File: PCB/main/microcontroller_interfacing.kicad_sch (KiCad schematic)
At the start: 12 parts, among them IC3 M24C02-WMN6TP, J6 Conn_01x01_Female, J7 Conn_01x01_Female, J8 Conn_01x01_Female, U4 CH340G, Y1 Crystal

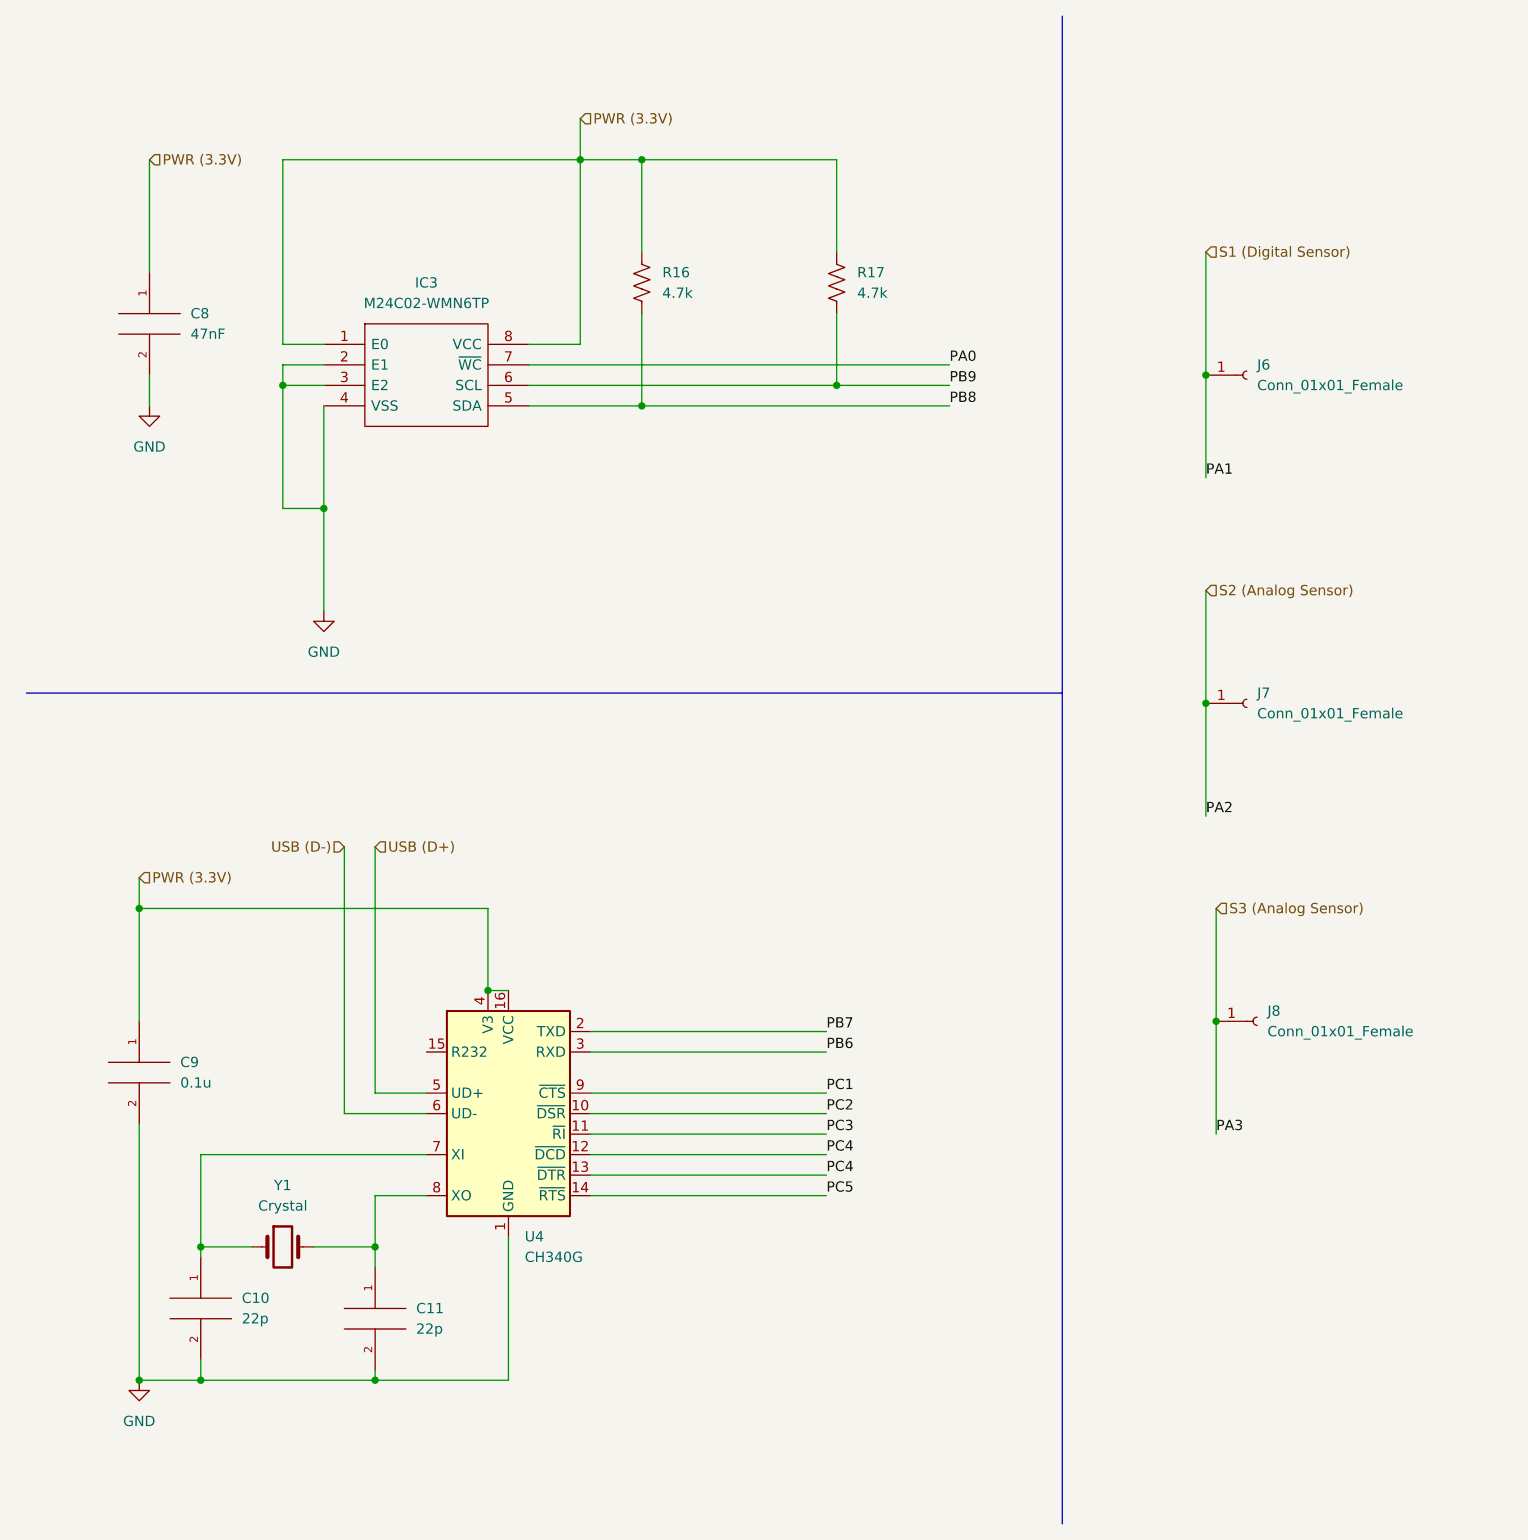
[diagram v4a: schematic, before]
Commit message: Power v0.1, Sensing v0.1, uC Control v0.1, ERC
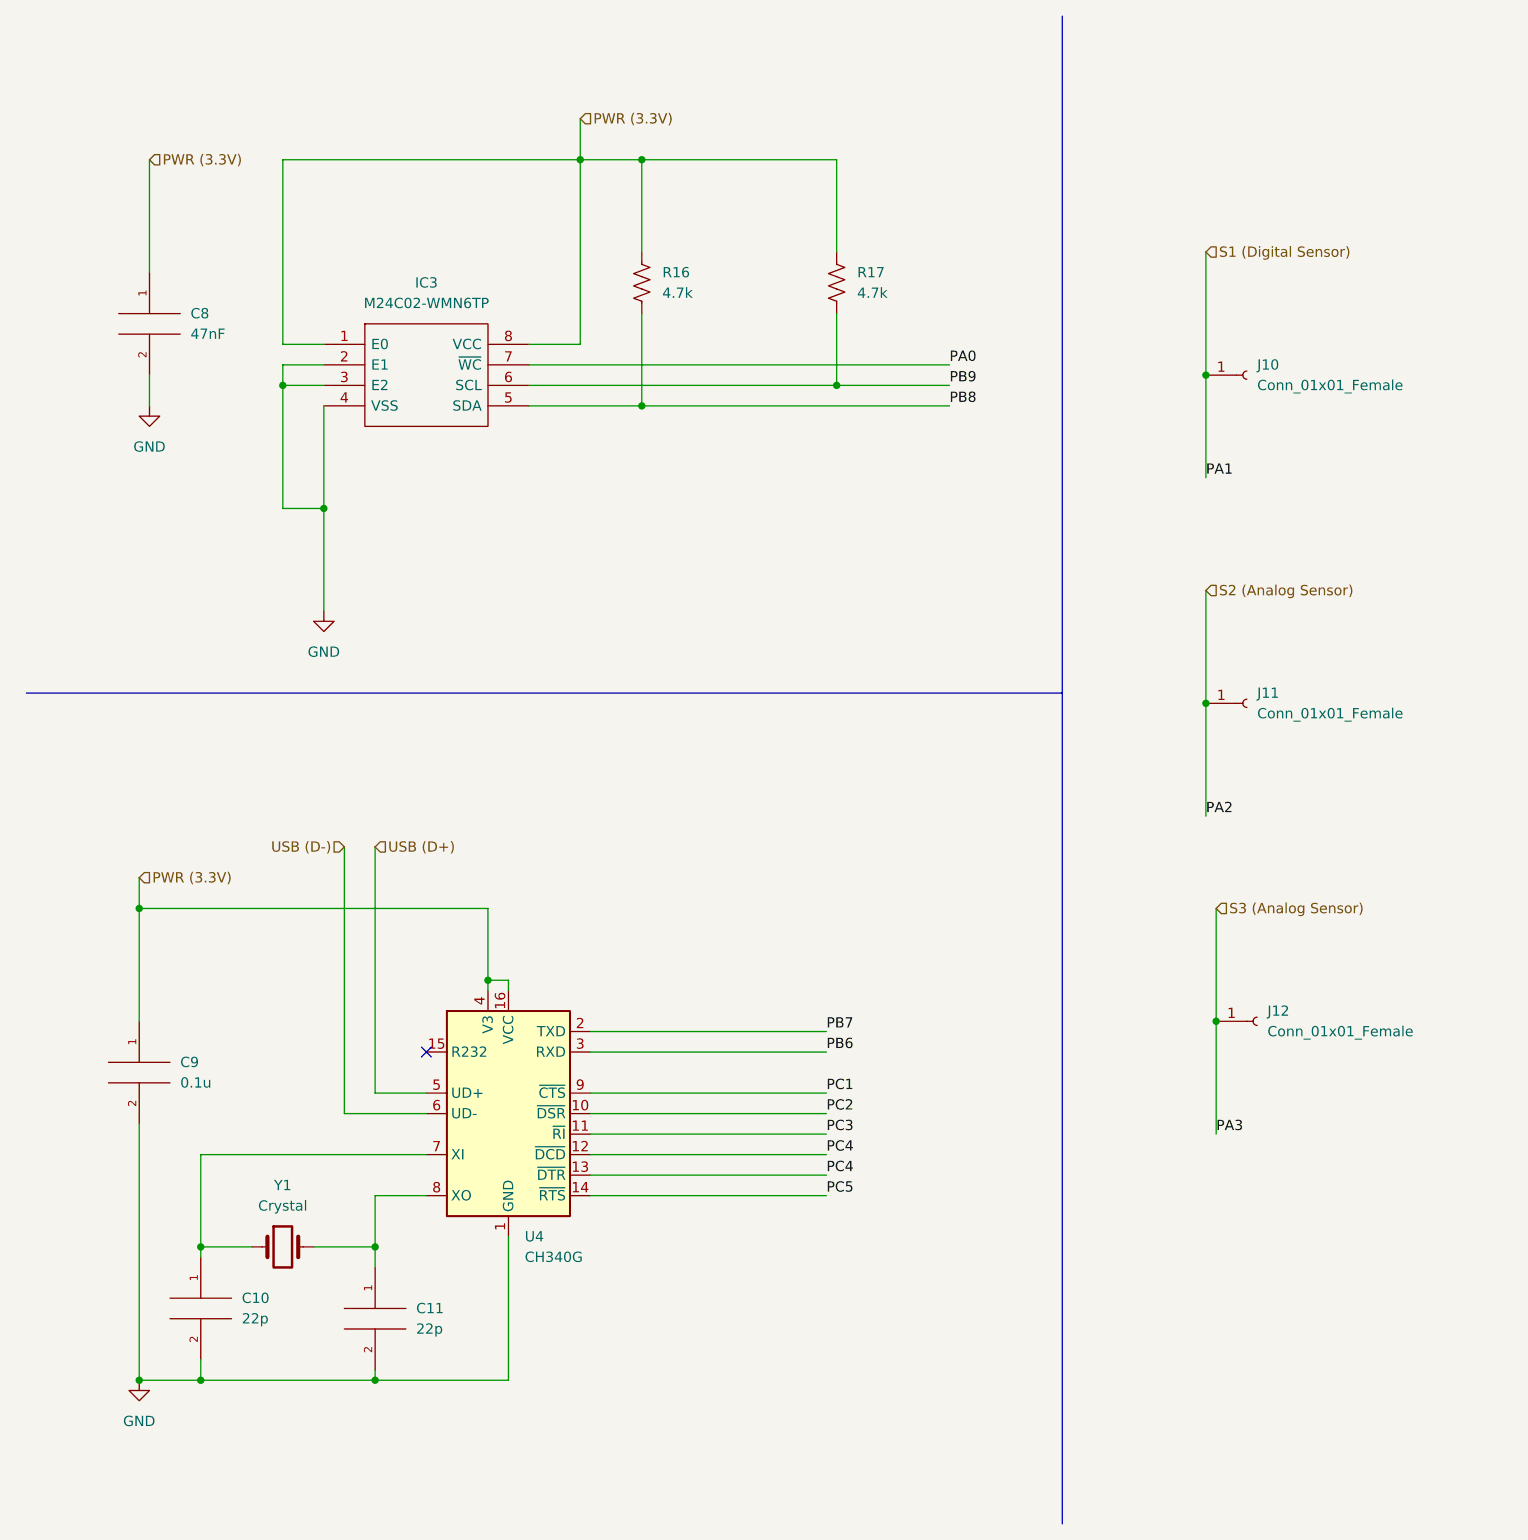
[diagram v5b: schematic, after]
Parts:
- renumbered J6 to J10, J7 to J11, J8 to J12
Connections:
- no-connect marks 0 -> 1
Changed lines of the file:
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@@
   (junction (at 157.48 55.88) (diameter 0) (color 0 0 0 0)
   )
+  (junction (at 68.58 130.81) (diameter 0) (color 0 0 0 0)
+  )
   (junction (at 111.76 57.15) (diameter 0) (color 0 0 0 0)
   )
   (junction (at 80.01 29.21) (diameter 0) (color 0 0 0 0)
   )
-  (junction (at 68.58 132.08) (diameter 0) (color 0 0 0 0)
-  )
   (junction (at 25.4 180.34) (diameter 0) (color 0 0 0 0)
   )
@@
   (junction (at 54.61 180.34) (diameter 0) (color 0 0 0 0)
   )
+  (no_connect (at 60.96 139.7))
   (wire (pts (xy 48.26 52.07) (xy 43.18 52.07))
     (stroke (width 0) (type default) (color 0 0 0 0))
@@
     (stroke (width 0) (type default) (color 0 0 0 0))
   )
-  (wire (pts (xy 68.58 132.08) (xy 71.12 132.08))
-    (stroke (width 0) (type default) (color 0 0 0 0))
-  )
   (wire (pts (xy 111.76 29.21) (xy 87.63 29.21))
     (stroke (width 0) (type default) (color 0 0 0 0))
@@
     (stroke (width 0) (type default) (color 0 0 0 0))
   )
+  (wire (pts (xy 71.12 130.81) (xy 71.12 132.08))
+    (stroke (width 0) (type default) (color 0 0 0 0))
+  )
   (wire (pts (xy 33.02 163.83) (xy 39.37 163.83))
     (stroke (width 0) (type default) (color 0 0 0 0))
@@
     (stroke (width 0) (type default) (color 0 0 0 0))
   )
-  (wire (pts (xy 68.58 121.92) (xy 68.58 132.08))
+  (wire (pts (xy 68.58 121.92) (xy 68.58 130.81))
     (stroke (width 0) (type default) (color 0 0 0 0))
   )
@@
     (stroke (width 0) (type default) (color 0 0 0 0))
   )
+  (wire (pts (xy 68.58 130.81) (xy 71.12 130.81))
+    (stroke (width 0) (type default) (color 0 0 0 0))
+  )
   (wire (pts (xy 81.28 152.4) (xy 110.49 152.4))
     (stroke (width 0) (type default) (color 0 0 0 0))
@@
   )
   (wire (pts (xy 46.99 163.83) (xy 54.61 163.83))
+    (stroke (width 0) (type default) (color 0 0 0 0))
+  )
+  (wire (pts (xy 68.58 130.81) (xy 68.58 132.08))
     (stroke (width 0) (type default) (color 0 0 0 0))
   )
@@
   (symbol (lib_id "power:GND") (at 26.67 59.69 0) (unit 1)
     (in_bom yes) (on_board yes) (fields_autoplaced)
-    (property "Reference" "#PWR038" (id 0) (at 26.67 66.04 0)
+    (property "Reference" "#PWR040" (id 0) (at 26.67 66.04 0)
       (effects (font (size 1.27 1.27)) hide)
     )
@@
   (symbol (lib_id "power:GND") (at 25.4 180.34 0) (unit 1)
     (in_bom yes) (on_board yes) (fields_autoplaced)
-    (property "Reference" "#PWR040" (id 0) (at 25.4 186.69 0)
+    (property "Reference" "#PWR042" (id 0) (at 25.4 186.69 0)
       (effects (font (size 1.27 1.27)) hide)
     )
@@
   (symbol (lib_id "Connector:Conn_01x01_Female") (at 162.56 96.52 0) (unit 1)
     (in_bom yes) (on_board yes) (fields_autoplaced)
-    (property "Reference" "J7" (id 0) (at 163.83 95.2499 0)
+    (property "Reference" "J11" (id 0) (at 163.83 95.2499 0)
       (effects (font (size 1.27 1.27)) (justify left))
     )
@@
   (symbol (lib_id "Connector:Conn_01x01_Female") (at 163.83 135.89 0) (unit 1)
     (in_bom yes) (on_board yes) (fields_autoplaced)
-    (property "Reference" "J8" (id 0) (at 165.1 134.6199 0)
+    (property "Reference" "J12" (id 0) (at 165.1 134.6199 0)
       (effects (font (size 1.27 1.27)) (justify left))
     )
@@
   (symbol (lib_id "Connector:Conn_01x01_Female") (at 162.56 55.88 0) (unit 1)
     (in_bom yes) (on_board yes) (fields_autoplaced)
-    (property "Reference" "J6" (id 0) (at 163.83 54.6099 0)
+    (property "Reference" "J10" (id 0) (at 163.83 54.6099 0)
       (effects (font (size 1.27 1.27)) (justify left))
     )
@@
   (symbol (lib_id "power:GND") (at 48.26 85.09 0) (unit 1)
     (in_bom yes) (on_board yes) (fields_autoplaced)
-    (property "Reference" "#PWR039" (id 0) (at 48.26 91.44 0)
-      (effects (font (size 1.27 1.27)) hide)
-    )
+    (property "Reference" "#PWR041" (id 0) (at 48.26 91.44 0)
+      (effects (font (size 1.27 1.27)) hide)
+    )

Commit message: Schematic updates
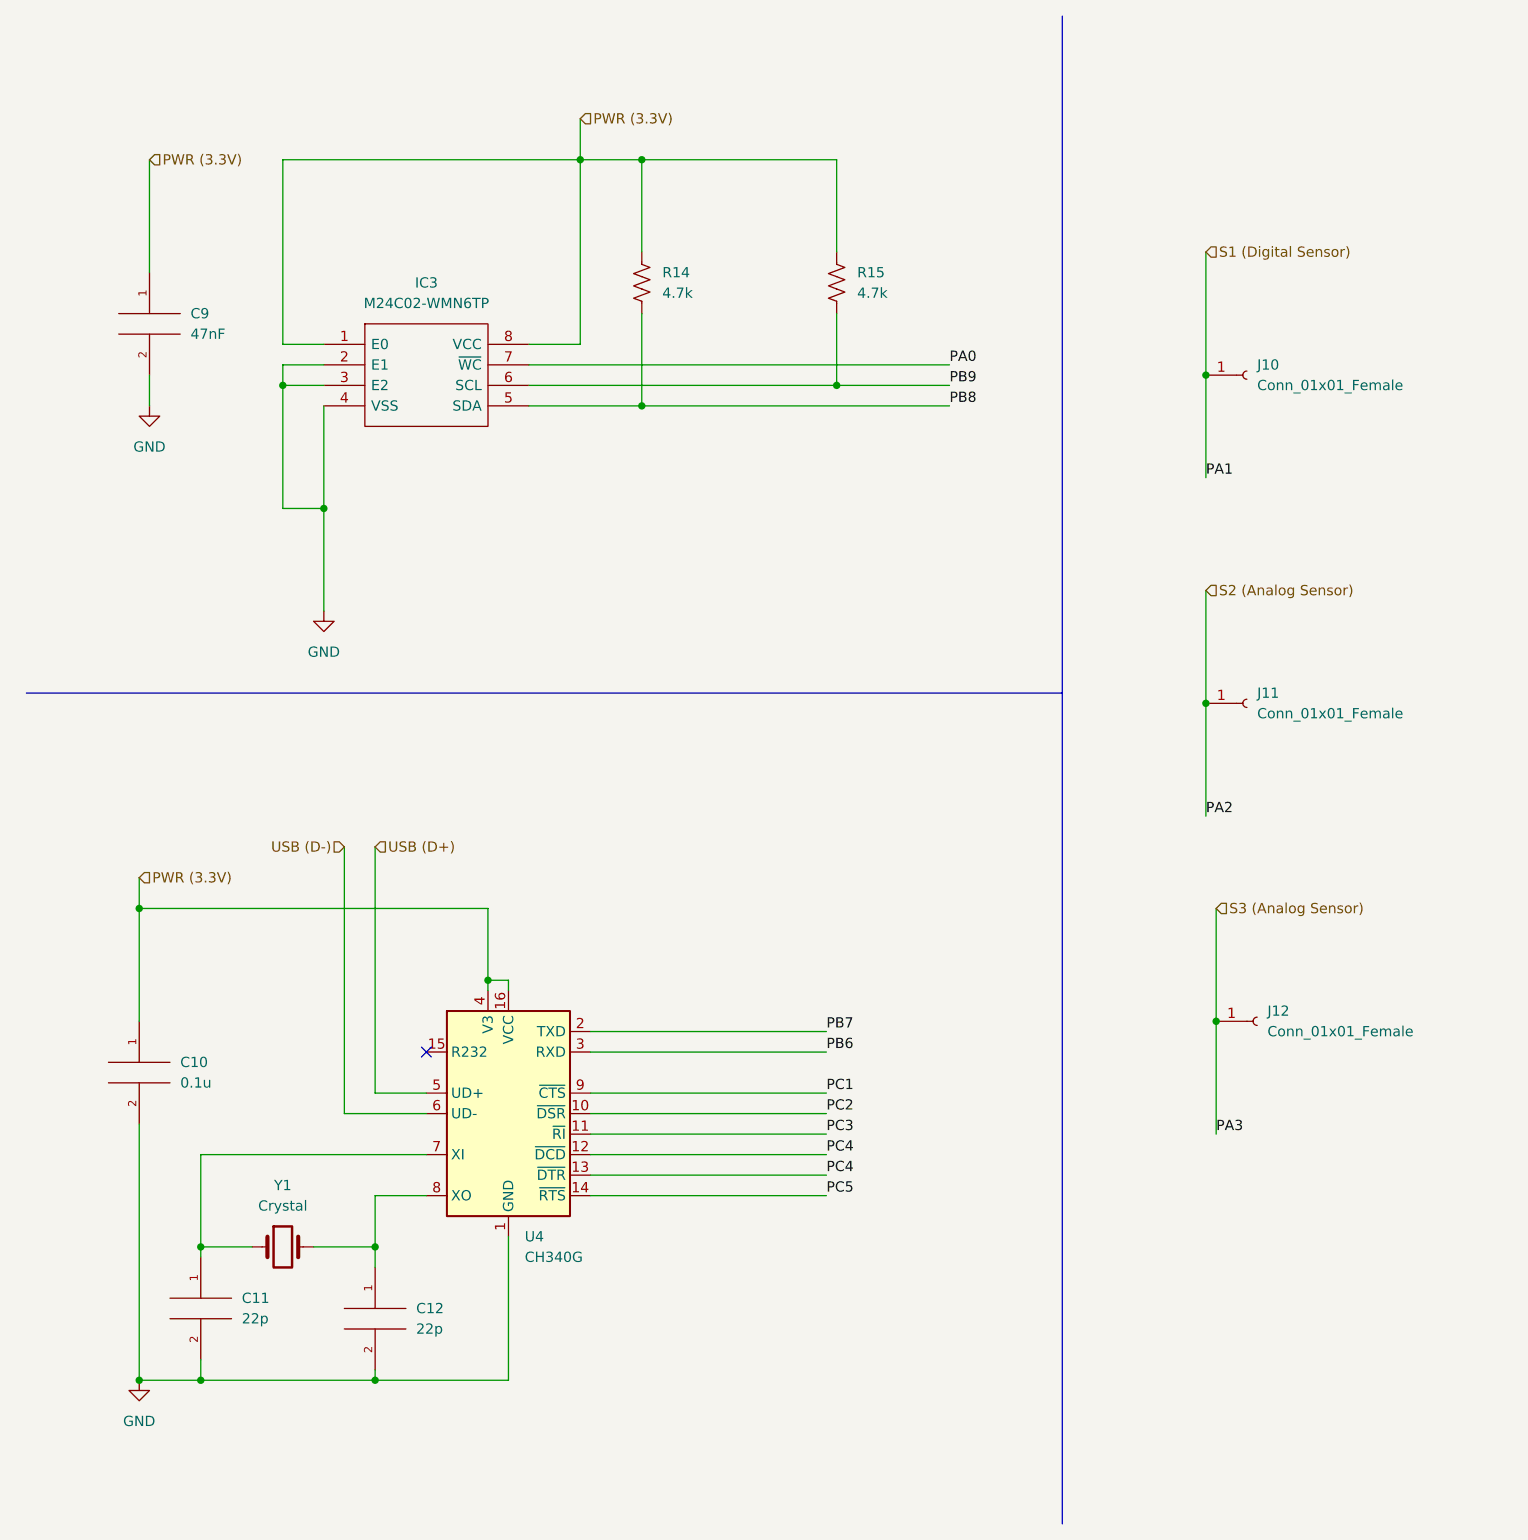
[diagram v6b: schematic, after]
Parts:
- renumbered C9 to C10, C10 to C11, C11 to C12, C8 to C9, R16 to R14, R17 to R15
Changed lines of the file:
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@@
   (symbol (lib_id "pspice:CAP") (at 33.02 171.45 0) (unit 1)
     (in_bom yes) (on_board yes) (fields_autoplaced)
-    (property "Reference" "C10" (id 0) (at 38.1 170.1799 0)
+    (property "Reference" "C11" (id 0) (at 38.1 170.1799 0)
       (effects (font (size 1.27 1.27)) (justify left))
     )
@@
   (symbol (lib_id "power:GND") (at 26.67 59.69 0) (unit 1)
     (in_bom yes) (on_board yes) (fields_autoplaced)
-    (property "Reference" "#PWR040" (id 0) (at 26.67 66.04 0)
+    (property "Reference" "#PWR041" (id 0) (at 26.67 66.04 0)
       (effects (font (size 1.27 1.27)) hide)
     )
@@
   (symbol (lib_id "pspice:CAP") (at 54.61 172.72 0) (unit 1)
     (in_bom yes) (on_board yes) (fields_autoplaced)
-    (property "Reference" "C11" (id 0) (at 59.69 171.4499 0)
+    (property "Reference" "C12" (id 0) (at 59.69 171.4499 0)
       (effects (font (size 1.27 1.27)) (justify left))
     )
@@
   (symbol (lib_id "power:GND") (at 25.4 180.34 0) (unit 1)
     (in_bom yes) (on_board yes) (fields_autoplaced)
-    (property "Reference" "#PWR042" (id 0) (at 25.4 186.69 0)
+    (property "Reference" "#PWR043" (id 0) (at 25.4 186.69 0)
       (effects (font (size 1.27 1.27)) hide)
     )
@@
   (symbol (lib_id "pspice:CAP") (at 26.67 49.53 0) (unit 1)
     (in_bom yes) (on_board yes) (fields_autoplaced)
-    (property "Reference" "C8" (id 0) (at 31.75 48.2599 0)
+    (property "Reference" "C9" (id 0) (at 31.75 48.2599 0)
       (effects (font (size 1.27 1.27)) (justify left))
     )
@@
   (symbol (lib_id "pspice:CAP") (at 25.4 142.24 0) (unit 1)
     (in_bom yes) (on_board yes) (fields_autoplaced)
-    (property "Reference" "C9" (id 0) (at 30.48 140.9699 0)
+    (property "Reference" "C10" (id 0) (at 30.48 140.9699 0)
       (effects (font (size 1.27 1.27)) (justify left))
     )
@@
   (symbol (lib_id "power:GND") (at 48.26 85.09 0) (unit 1)
     (in_bom yes) (on_board yes) (fields_autoplaced)
-    (property "Reference" "#PWR041" (id 0) (at 48.26 91.44 0)
+    (property "Reference" "#PWR042" (id 0) (at 48.26 91.44 0)
       (effects (font (size 1.27 1.27)) hide)
     )
@@
   (symbol (lib_id "Device:R_US") (at 111.76 44.45 0) (unit 1)
     (in_bom yes) (on_board yes) (fields_autoplaced)
-    (property "Reference" "R17" (id 0) (at 114.3 43.1799 0)
+    (property "Reference" "R15" (id 0) (at 114.3 43.1799 0)
       (effects (font (size 1.27 1.27)) (justify left))
     )
@@
   (symbol (lib_id "Device:R_US") (at 87.63 44.45 0) (unit 1)
     (in_bom yes) (on_board yes) (fields_autoplaced)
-    (property "Reference" "R16" (id 0) (at 90.17 43.1799 0)
-      (effects (font (size 1.27 1.27)) (justify left))
-    )
+    (property "Reference" "R14" (id 0) (at 90.17 43.1799 0)
+      (effects (font (size 1.27 1.27)) (justify left))
+    )
